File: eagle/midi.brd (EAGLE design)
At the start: 62.5 x 83.8 mm, 31 parts, among them CON1 EXPANSION-PORT, IC1 74LS14, IC2 6N138, IC4 74LS02, IC5 74LS74, IC6 74AHCT1G32DBV, IC7 74LS273, IC8 SST39SF040, IC9 74LS00D, Q1 2MHz

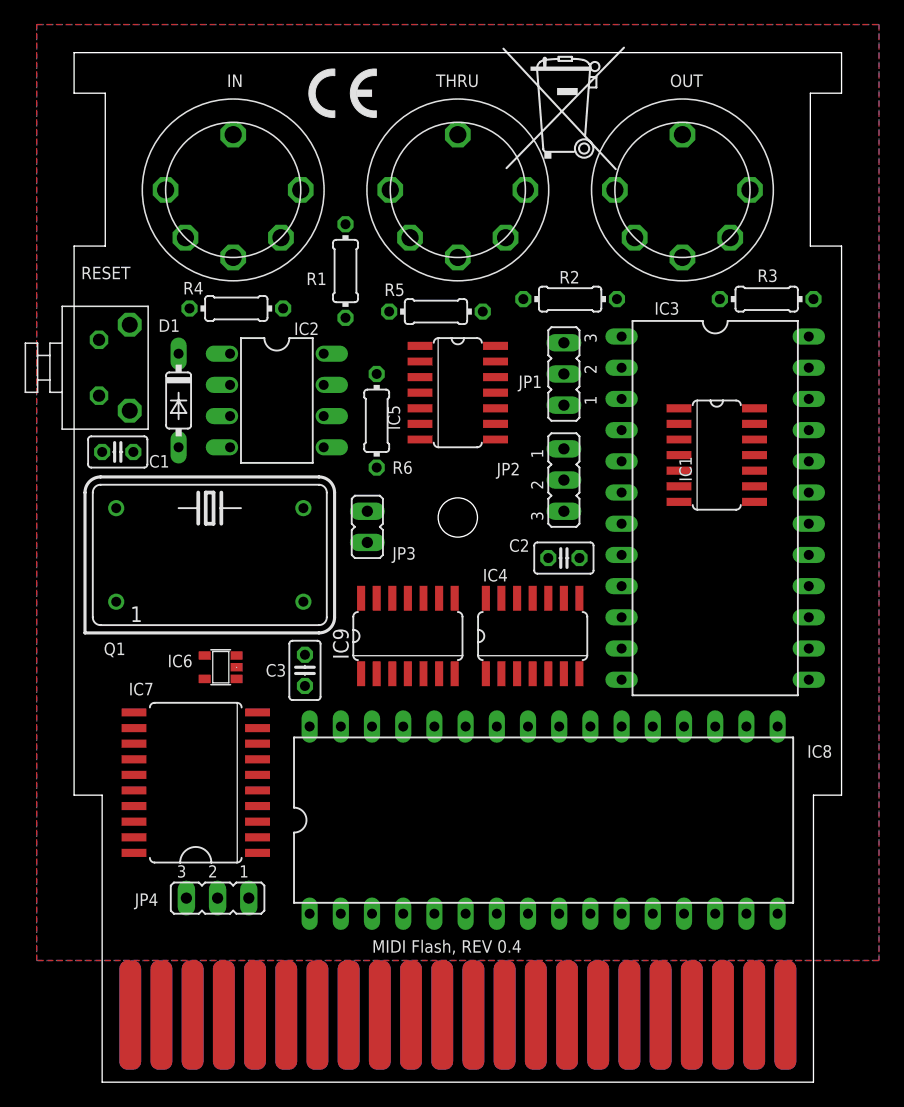
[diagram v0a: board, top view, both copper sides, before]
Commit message: version 0.5 with additonal 74LS00
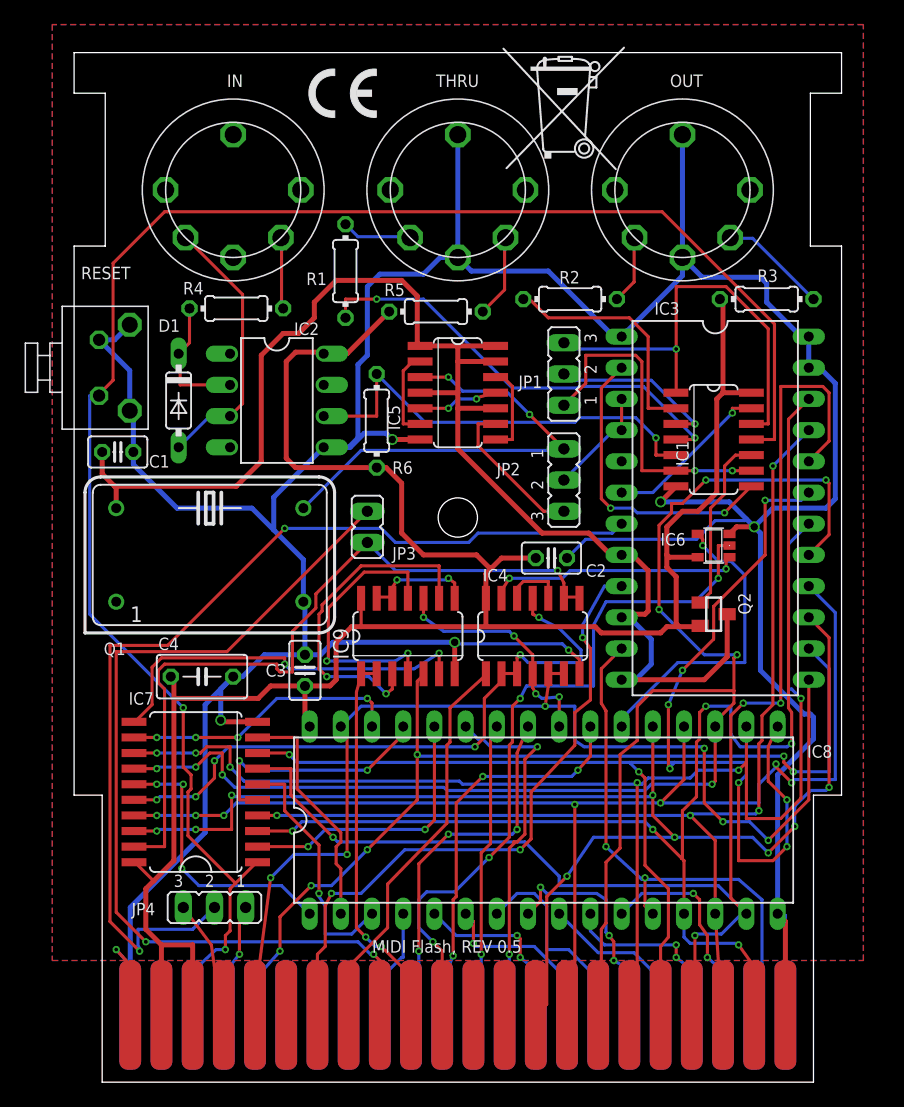
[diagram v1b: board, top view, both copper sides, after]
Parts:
- added C4: 10u, rcl:C050-035X075
- added Q2: DMP2100U, transistor-power:SUPER-SOT3
- moved IC6 41.3 mm to (50.0, 43.9)
- moved IC1 1.30 mm to (50.0, 52.6)
- moved C2 1.02 mm to (36.8, 42.9), turned to 0 degrees
- moved JP4 0.80 mm to (9.40, 14.5)
- moved IC7 0.76 mm to (7.87, 23.9)
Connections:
- removed net OE: IC4.4, IC8.24
- removed net ROMH: CON1.B
- new net !RW: IC4.4, IC8.24, IC9.10
- new net 5V-SW: C1.1, IC3.10, IC3.12, IC3.8, IC5.1, IC5.10, IC5.13, IC5.14, IC5.4, Q1.14, Q2.3
- new net N$30: IC9.11, IC9.4
- new net N$35: IC1.10, Q2.1
- new net N$9: IC9.12, IC9.13, IC9.8
- net +5V: now also C4.1, Q2.2; no longer C1.1, IC3.10, IC3.12, IC3.8, IC5.1, IC5.10, IC5.13, IC5.14, IC5.4, Q1.14
- net GND: now also C4.2; no longer IC1.11, IC9.10, IC9.12, IC9.13, IC9.9
- net N$8: now also IC9.9; no longer IC9.4
- net RESET: now also IC1.11
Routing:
- net GND: track 0.00 -> 318.6 mm, vias 0 -> 7
- net +5V: track 0.00 -> 177.3 mm
- net RESET: track 0.00 -> 142.7 mm, vias 0 -> 2
- net D5: track 0.00 -> 133.6 mm, vias 0 -> 8
- net 5V-SW: track 0.00 -> 117.1 mm
- net D2: track 0.00 -> 115.3 mm, vias 0 -> 4
- net D3: track 0.00 -> 115.0 mm, vias 0 -> 9
- net D7: track 0.00 -> 108.5 mm, vias 0 -> 9
- net D4: track 0.00 -> 108.5 mm, vias 0 -> 6
- net D0: track 0.00 -> 105.3 mm, vias 0 -> 5
- net D6: track 0.00 -> 102.0 mm, vias 0 -> 7
- net RW: track 0.00 -> 91.5 mm, vias 0 -> 6
- net D1: track 0.00 -> 90.8 mm, vias 0 -> 4
- net IRQ: track 0.00 -> 81.4 mm, vias 0 -> 2
- net S02: track 0.00 -> 79.5 mm, vias 0 -> 6
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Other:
- board text added: "MIDI Flash, REV 0.5"
- board text removed: "MIDI Flash, REV 0.4"

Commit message: revision 1.0
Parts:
- added C10, C5, C6, C7, C8, C9: 100n, rcl:C0805
- added C11, C12: 1n, rcl:C0805
- added D2, D3: BAV99, diode:SOT23
- added R7: 10k, rcl:R0805
- C1, C2, C3: device rcl:C025-025X050 -> rcl:C0805
- C4: device rcl:C050-035X075 -> rcl:C0805
- D1: value 1N914 -> BAV99; device diode:DO35-7 -> diode:SOT23
- R1, R2, R3, R4, R5, R6: device rcl:0204/7 -> rcl:R1206
- moved C1 46.4 mm to (43.7, 32.3)
- moved C2 21.9 mm to (52.1, 58.7), turned to 180 degrees
- moved C3 19.8 mm to (4.06, 18.5), turned to 0 degrees
- moved C4 19.4 mm to (2.79, 14.7), turned to 270 degrees
- moved U$1 17.3 mm to (49.5, 74.2)
- moved U$2 16.0 mm to (1.02, 79.5)
- moved R6 3.34 mm to (22.1, 57.4), turned to 90 degrees
- moved IC7 2.79 mm to (7.87, 26.7)
- moved R5 2.54 mm to (24.9, 63.1)
- moved R3 2.18 mm to (55.6, 65.8)
- moved IC3 2.04 mm to (50.0, 49.0)
- moved R2 1.78 mm to (38.4, 65.8), turned to 270 degrees
- moved IC6 1.78 mm to (50.0, 45.7)
- moved D1 1.40 mm to (6.35, 57.1), turned to 0 degrees
- moved Q2 1.37 mm to (48.8, 38.9), turned to 180 degrees
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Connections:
- removed net N$2: D1.C, IC2.2, R4.1
- new net N$37: D1.2, D1.3, IC2.2, R4.1
- net +5V: now also C10.1, C7.1, C8.1, C9.1, D2.2, D3.2, R7.1
- net 5V-SW: now also C5.1, C6.1
- net GND: now also C10.2, C11.2, C12.2, C5.2, C6.2, C7.2, C8.2, C9.2, D2.1, D3.1
- net N$16: now also C12.1, D3.3
- net N$28: now also C11.1, D2.3
- net N$3: now also D1.1; no longer D1.A
- net N$35: now also R7.2
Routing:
- net GND: track 318.6 -> 509.2 mm, vias 7 -> 23
- net N$22: track 22.9 -> 78.1 mm, vias 3 -> 6
- net +5V: track 177.3 -> 232.1 mm
- net D1: track 90.8 -> 133.5 mm, vias 4 -> 8
- net EXROM: track 73.9 -> 45.7 mm, vias 2 -> 4
- net N$5: track 27.4 -> 53.5 mm, vias 2 -> 3
- net D7: track 108.5 -> 83.2 mm, vias 9 -> 8
- net D5: track 133.6 -> 108.7 mm, vias 8 -> 7
- net N$37: track 0.00 -> 24.2 mm
- net N$28: track 5.72 -> 28.2 mm, vias 0 -> 2
- net N$23: track 31.5 -> 52.4 mm, vias 2 -> 4
- net N$16: track 5.60 -> 24.7 mm, vias 0 -> 1
- net N$12: track 36.4 -> 53.7 mm
- net RESET: track 142.7 -> 127.3 mm, vias 2 -> 10
- net D3: track 115.0 -> 99.8 mm, vias 9 -> 3
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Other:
- board text added: "FRANK-BUSS.DE"
- board text added: "KERBEROS, REV 1.0"
- board text removed: "MIDI Flash, REV 0.5"

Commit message: circuit rev B with CPLD
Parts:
- removed C10, C2, C5, C6, C7, C8, C9: 100n, rcl:C0805
- removed C11, C12: 1n, rcl:C0805
- removed C4: 10u, rcl:C0805
- removed D1, D2, D3: BAV99, diode:SOT23
- removed IC6: 74AHCT1G32DBV, 74xx-little-de:SOT23-5
- removed IC7: 74LS273, 74xx-eu:SO20W
- removed IC8: SST39SF040, flash:DIL32
- removed IC9: 74LS00D, 74xx-eu:SO14
- removed JP2, JP4: (no value), jumper:JP2
- removed JP3: (no value), jumper:JP1
- removed Q1: 2MHz, crystal:DIL14S
- removed Q2: DMP2100U, transistor-power:SUPER-SOT3
- added 3V3, AUX, GND, TCK, TDI, TDO, TMS: LSP10, solpad:LSP10
- added C13, C14, C17, C18, C19, C20, C21, C26, C28, C37: 100n, rcl:C0402
- added C15, C16: 1n, rcl:C0402
- added C22: 10u, rcl:C0805
- added C24: 1u, rcl:C0805
- added D4, D5, D6: BAV99, diode:SOT23
- added IC11: (no value), micro-motorola:DIL24
- added IC12: 74LS14, 74xx-eu:SO14
- added IC16: 74LVC8T245, 74lvc8t245:TSSOP24
- added IC18: MCP1703CB, linear:SOT23
- added LED1, LED2: (no value), led:LED3MM
- added R10, R11, R12, R13, R8, R9: 220, rcl:R1206
- added R14, R17, R18: 10k, rcl:R0402
- added R15, R16: 4k7, rcl:R0402
- C1, C3: device rcl:C0805 -> rcl:C0402
- IC1: value 74LS14 -> SST39VF1681; device 74xx-eu:SO14 -> flash:TSOP48
- IC2: value 6N138 -> XC9572XL_TQ100; device optocoupler:DIL08 -> xc9572xl-tq100:TQ100
- IC3: value (none) -> 6N138SMD; device micro-motorola:DIL24 -> 6n138:SO8-GW300
- IC4: value 74LS02 -> 12MHz; device 74xx-eu:SO14 -> cartridge:ASE
- IC5: value 74LS74 -> CY61228EV30; device 74xx-eu:SO14 -> CY62128EV30:TSOP8X16
- JP1: device jumper:JP2 -> jumper:JP1
- R1, R2, R3: value 220 -> 10k; device rcl:R1206 -> rcl:R0402
- R4, R5: value 220 -> 1k; device rcl:R1206 -> rcl:R0402
- R6: value 330 -> 10k; device rcl:R1206 -> rcl:R0402
- R7: value 10k -> 220; device rcl:R0805 -> rcl:R1206
- moved JP1 49.0 mm to (18.4, 12.9), turned to 270 degrees
- moved R1 47.4 mm to (3.05, 23.4)
- moved IC3 39.6 mm to (10.7, 52.8), turned to 0 degrees
- moved IC5 34.6 mm to (51.1, 29.2), turned to 180 degrees
- moved IC2 34.2 mm to (34.0, 27.7), turned to 90 degrees
- moved R7 33.9 mm to (20.3, 50.8), turned to 270 degrees
- moved C3 22.9 mm to (23.7, 30.2), turned to 270 degrees
- moved R2 14.9 mm to (52.3, 60.7), turned to 0 degrees
- moved R5 13.3 mm to (38.1, 61.5)
- moved IC4 13.2 mm to (37.8, 49.5), turned to 270 degrees
- moved C1 12.8 mm to (56.4, 30.5), turned to 270 degrees
- moved R4 9.43 mm to (19.8, 61.5), turned to 180 degrees
- moved R6 6.31 mm to (17.3, 53.3)
- moved R3 5.08 mm to (55.6, 60.7), turned to 0 degrees
- moved IC1 4.10 mm to (51.6, 49.0), turned to 90 degrees
- renumbered CON1 to CON2, RESET to RESET1
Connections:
- removed net !RW: IC4.4, IC8.24, IC9.10
- removed net 5V-SW: C1.1, C5.1, C6.1, IC3.10, IC3.12, IC3.8, IC5.1, IC5.10, IC5.13, IC5.14, IC5.4, Q1.14, Q2.3
- removed net CE: IC6.4, IC8.22
- removed net N$10: IC1.2, R2.2
- removed net N$11: IC1.3, JP1.2
- removed net N$12: IC1.4, R1.2
- removed net N$14: IC3.3, IC3.4, JP2.2
- removed net N$15: IC1.8, IC3.2
- removed net N$16: C12.1, D3.3, OUT.5, R2.1
- removed net N$17: IC7.2, IC8.28
- removed net N$19: IC7.6, IC8.3
- removed net N$20: IC7.9, IC8.2
- removed net N$21: IC7.12, IC8.30
- removed net N$22: IC7.15, IC8.1
- removed net N$23: IC7.11, IC9.6
- removed net N$24: IC4.10, IC4.12
- removed net N$25: IC1.13, IC3.6
- removed net N$26: CON2.4, JP4.3
- removed net N$27: CON2.D, JP4.1
- removed net N$28: C11.1, D2.3, R1.1, THRU.5
- removed net N$29: IC4.13, IC6.1
- removed net N$30: IC9.11, IC9.4
- removed net N$31: IC5.2, IC5.6
- removed net N$32: IC5.12, IC5.8
- removed net N$33: IC5.3, JP2.1, Q1.8
- removed net N$34: IC5.11, IC5.5
- removed net N$35: IC1.10, Q2.1, R7.2
- removed net N$36: IC5.9, JP2.3
- removed net N$37: D1.2, D1.3, IC2.2, R4.1
- removed net N$9: IC9.12, IC9.13, IC9.8
- removed net Q7: IC4.11, IC4.2, IC4.3, IC7.16
- removed net Q8: IC4.8, IC4.9, IC7.19, JP3.1
- new net +3V3: 3V3.MP, C1.1, C17.1, C18.1, C19.1, C24.1, C26.1, C28.1, C3.1, C37.1, IC1.12, IC1.37, IC16.1, IC18.2, IC2.26, IC2.38, IC2.5, IC2.51, IC2.57, IC2.88, IC2.98, IC4.4, IC5.6, IC5.8, R14.2, R15.1, R16.1, R18.2, R2.1
- new net 6850-CS2: IC11.9, IC2.63, R1.1
- new net 6850-IRQ: IC11.7, IC2.58
- new net 6850-RS: IC11.11, IC2.64
- new net 6850-RW: IC11.13, IC2.65
- new net 6850-RX/TX-CLK: IC11.3, IC11.4, IC2.55
- new net 6850-RXDATA: IC11.2, IC12.6, IC2.54
- new net 6850-TXDATA: IC11.6, IC12.3, IC2.56
- new net A13: CON2.J, IC2.77
- new net A14: CON2.H, IC2.74
- new net A15: CON2.F, IC2.71
- new net AT0: IC1.45, IC2.14, IC5.20
- new net AT1: IC1.25, IC2.13, IC5.19
- new net AT10: IC1.7, IC2.16, IC5.31
- new net AT11: IC1.6, IC2.22, IC5.11
- new net AT12: IC1.5, IC2.23, IC5.12
- new net AT13: IC1.4, IC2.25, IC5.13
- new net AT14: IC1.3, IC2.28, IC5.14
- new net AT15: IC1.2, IC2.29, IC5.15
- new net AT16: IC1.1, IC2.30, IC5.16
- new net AT17: IC1.48, IC2.59
- new net AT18: IC1.17, IC2.37
- new net AT19: IC1.16, IC2.36
- new net AT2: IC1.24, IC2.12, IC5.18
- new net AT20: IC1.9, IC2.33
- new net AT3: IC1.23, IC2.11, IC5.17
- new net AT4: IC1.22, IC2.20, IC5.10
- new net AT5: IC1.21, IC2.42, IC5.1
- new net AT6: IC1.20, IC2.41, IC5.2
- new net AT7: IC1.19, IC2.40, IC5.3
- new net AT8: IC1.18, IC2.39, IC5.4
- new net AT9: IC1.8, IC2.32, IC5.7
- new net BA: CON2.12
- new net DIR: IC16.2, IC2.1, R17.1
- new net DMA: CON2.13
- new net DOT-CLOCK: CON2.6
- new net DT0: IC1.29, IC16.3, IC2.3, IC5.29
- new net DT1: IC1.31, IC16.4, IC2.4, IC5.28
- new net DT2: IC1.33, IC16.5, IC2.6, IC5.27
- new net DT3: IC1.35, IC16.6, IC2.8, IC5.26
- new net DT4: IC1.38, IC16.7, IC2.9, IC5.25
- new net DT5: IC1.40, IC16.8, IC2.10, IC5.23
- new net DT6: IC1.42, IC16.9, IC2.18, IC5.22
- new net DT7: IC1.44, IC16.10, IC2.17, IC5.21
- new net FLASH-CE: IC1.26, IC2.60, R14.1
- new net LED1: IC2.53, R4.1
- new net LED2: IC2.52, R5.1
- new net MIDI-OUT-INVERTED: IC12.4, IC12.9
- new net MIDI-THRU: IC12.13, IC2.49
- new net N$2: IC2.27, IC4.3
- new net N$38: IN.4, R8.2
- new net N$39: IC12.1, IC3.6, R7.2
- new net N$40: OUT.4, R11.1
- new net N$41: R10.1, THRU.4
- new net N$42: C16.1, D6.3, OUT.5, R13.1
- new net N$43: C15.1, D5.3, R12.1, THRU.5
- new net N$44: IC12.8, R13.2
- new net N$45: IC12.10, R12.2
- new net N$47: D4.1, IC3.3, IN.5
- new net N$48: D4.2, D4.3, IC3.2, R8.1
- new net NMI: CON2.D, IC2.68
- new net OE: IC1.28, IC2.61, IC5.32
- new net RAM-CE: IC2.15, IC5.30, R18.1
- new net ROMH: CON2.B, IC2.66
- new net TCK: IC2.48, TCK.MP
- new net TDI: IC2.45, R15.2, TDI.MP
- new net TDO: IC2.83, TDO.MP
- new net TMS: IC2.47, R16.2, TMS.MP
- new net WE: IC1.11, IC2.35, IC5.5
- net +5V: now also C13.1, C14.1, C20.1, C21.1, C22.1, D5.2, D6.2, IC11.10, IC11.12, IC11.8, IC12.14, IC16.23, IC16.24, IC18.3, IC3.8, R1.2, R10.2, R11.2, R9.1; no longer C10.1, C2.1, C3.1, C4.1, C7.1, C8.1, C9.1, D2.2, D3.2, IC1.14, IC2.8, IC4.14, IC6.5, IC7.20, IC8.32, IC9.14, Q2.2, R3.2, R5.2, R6.2, R7.1
- net A0: now also IC2.99; no longer IC3.11, IC8.12
- net A1: now also IC2.97; no longer IC8.11
- net A10: now also IC2.86; no longer IC8.23
- net A11: now also IC2.82; no longer IC8.25
- net A12: now also IC2.79; no longer IC8.4
- net A2: now also IC2.96; no longer IC8.10
- net A3: now also IC2.95; no longer IC8.9
- net A4: now also IC2.94; no longer IC8.8
- net A5: now also IC2.93; no longer IC8.7
- net A6: now also IC2.92; no longer IC8.6
- net A7: now also IC2.91; no longer IC8.5
- net A8: now also IC2.90; no longer IC8.27
- net A9: now also IC2.89; no longer IC8.26
- net D0: now also IC11.22, IC16.21; no longer IC3.22, IC7.3, IC8.13
- net D1: now also IC11.21, IC16.20; no longer IC3.21, IC7.4, IC8.14
- net D2: now also IC11.20, IC16.19; no longer IC3.20, IC7.7, IC8.15
- net D3: now also IC11.19, IC16.18; no longer IC3.19, IC7.8, IC8.17
- net D4: now also IC11.18, IC16.17; no longer IC3.18, IC7.13, IC8.18
- net D5: now also IC11.17, IC16.16; no longer IC3.17, IC7.14, IC8.19
- net D6: now also IC11.16, IC16.15; no longer IC3.16, IC7.17, IC8.20
- net D7: now also IC11.15, IC16.14; no longer IC3.15, IC7.18, IC8.21
- net EXROM: now also JP1.1; no longer JP3.2
- net GAME: now also IC2.78; no longer IC4.1
- net GND: now also C13.2, C14.2, C15.2, C16.2, C17.2, C18.2, C19.2, C20.2, C21.2, C22.2, C24.2, C26.2, C28.2, C37.2, D5.1, D6.1, GND.MP, IC1.27, IC1.46, IC11.1, IC11.23, IC11.24, IC12.7, IC16.11, IC16.12, IC16.13, IC16.22, IC18.1, IC2.100, IC2.21, IC2.31, IC2.44, IC2.62, IC2.69, IC2.75, IC2.84, IC3.5, IC4.2, IC5.24, LED1.K, LED2.K, R17.2, R3.2, R6.1; no longer C10.2, C11.2, C12.2, C2.2, C4.2, C5.2, C6.2, C7.2, C8.2, C9.2, D2.1, D3.1, IC1.7, IC2.5, IC3.1, IC3.23, IC3.24, IC4.7, IC5.7, IC6.3, IC7.10, IC8.16, IC9.7, Q1.7
- net IO1: now also IC2.76; no longer IC3.9
- net IO2: now also IC2.85; no longer IC9.1, IC9.2
- net IRQ: now also CON2.4, IC2.70; no longer IC3.7, JP4.2
- net N$1: now also IC3.7, R6.2; no longer IN.4, R4.2
- net N$13: now also IC1.14, R2.2, R3.1; no longer IC1.1, IC1.12, JP1.3
- net N$18: now also LED2.A, R5.2; no longer IC7.5, IC8.29
- net N$3: now also R7.1, R9.2; no longer D1.1, IC2.3, IN.5
- net N$4: now also IC12.11, IC12.12; no longer IC1.5, IC2.6, R6.1
- net N$5: now also IC12.2, IC12.5; no longer IC1.6, IC1.9, JP1.1
- net N$6: now also LED1.A, R4.2; no longer OUT.4, R3.1
- net N$7: now also IC2.81, JP1.2; no longer R5.1, THRU.4
- net N$8: now also AUX.MP, IC2.50; no longer IC9.3, IC9.9
- net RESET: now also IC2.67; no longer IC1.11, IC7.1
- net ROML: now also IC2.87; no longer IC6.2
- net RW: now also IC2.72; no longer IC3.13, IC4.5, IC4.6, IC8.31
- net S02: now also IC11.14; no longer IC3.14, IC9.5
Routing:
- net GND: track 509.2 -> 800.6 mm, vias 23 -> 34
- net +3V3: track 0.00 -> 230.4 mm, vias 0 -> 3
- net 5V-SW: track 117.5 -> 0.00 mm, vias 2 -> 0
- net N$22: track 78.1 -> 0.00 mm, vias 6 -> 0
- net D1: track 133.5 -> 57.5 mm, vias 8 -> 1
- net OE: track 0.00 -> 72.5 mm, vias 0 -> 5
- net S02: track 85.9 -> 18.0 mm, vias 4 -> 2
- net 6850-TXDATA: track 0.00 -> 64.4 mm, vias 0 -> 3
- net RW: track 91.7 -> 29.2 mm, vias 5 -> 0
- net D5: track 108.7 -> 46.4 mm, vias 7 -> 1
- net LED1: track 0.00 -> 61.8 mm, vias 0 -> 4
- net DT0: track 0.00 -> 60.1 mm, vias 0 -> 2
- net AT2: track 0.00 -> 59.7 mm, vias 0 -> 2
- net FLASH-CE: track 0.00 -> 58.8 mm, vias 0 -> 5
- net DT1: track 0.00 -> 58.3 mm, vias 0 -> 2
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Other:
- outline, holes or cut-outs redrawn
- board text added: "KERBEROS, REV B"
- board text removed: "KERBEROS, REV 1.0"

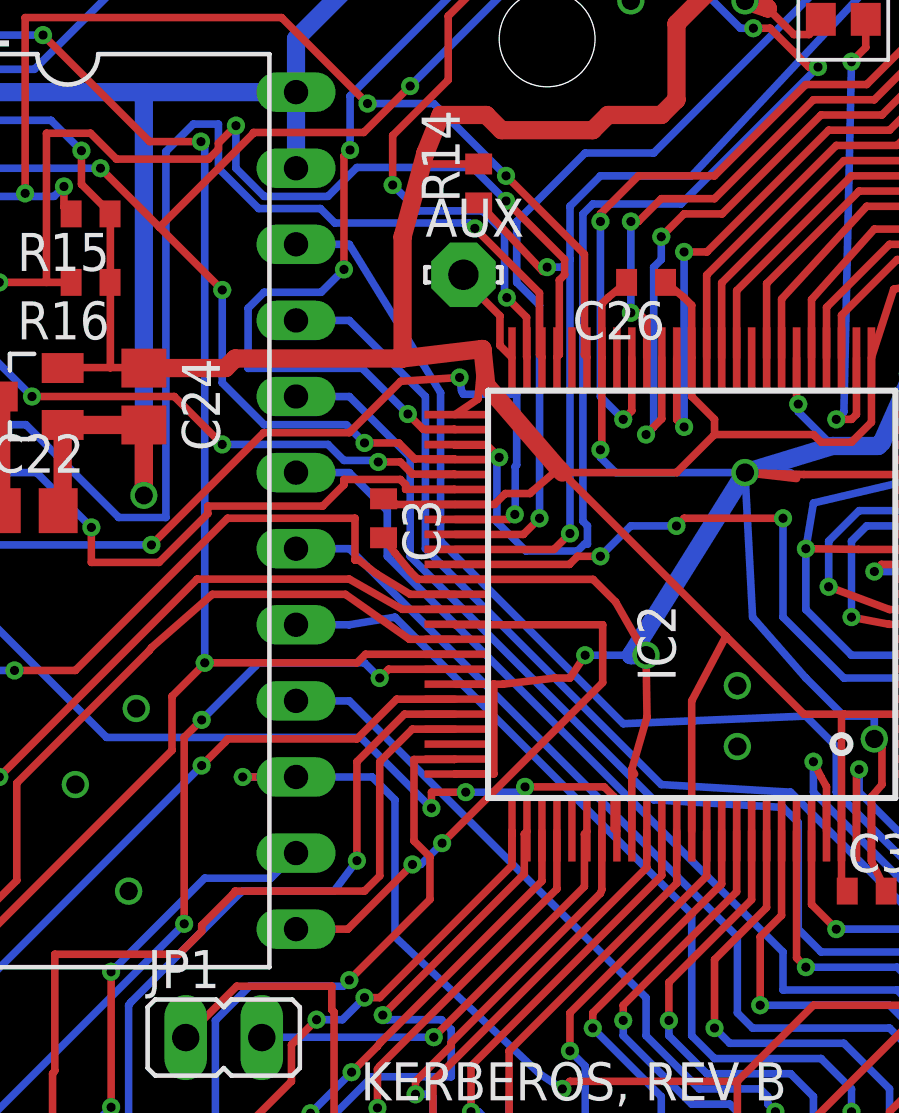
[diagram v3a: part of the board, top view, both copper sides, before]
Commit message: first working prototype with CPLD
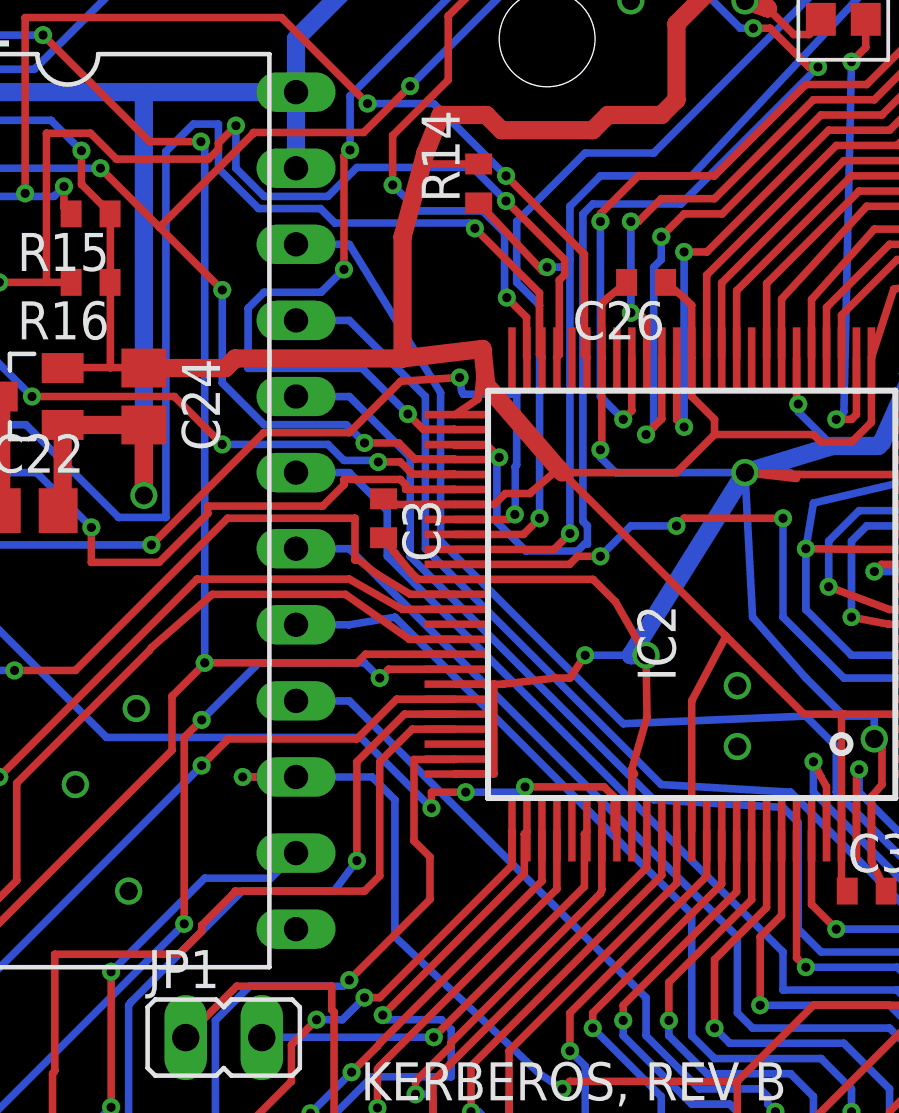
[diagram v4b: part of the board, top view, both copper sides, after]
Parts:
- removed AUX: LSP10, solpad:LSP10
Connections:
- removed net 6850-RW: IC11.13, IC2.65
- removed net N$8: AUX.MP, IC2.50
- net BA: now also IC2.65
- net RW: now also IC11.13
- net S02: now also IC2.50
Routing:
- net 6850-RW: track 20.5 -> 0.00 mm, vias 2 -> 0
- net N$8: track 3.44 -> 0.00 mm
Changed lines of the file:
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@@
 <element name="R14" library="rcl" package="R0402" value="10k" x="26.924" y="41.402" rot="R90"/>
 <element name="R18" library="rcl" package="R0402" value="10k" x="57.404" y="32.766"/>
-<element name="AUX" library="solpad" package="LSP10" value="LSP10" x="26.416" y="38.354"/>
 <element name="JP1" library="jumper" package="JP1" value="" x="18.415" y="12.8905" rot="R270"/>
 </elements>
@@
 <via x="14.6558" y="15.0876" extent="1-16" drill="0.3048"/>
 <via x="14.6558" y="10.5664" extent="1-16" drill="0.3048"/>
+<contactref element="IC2" pad="50"/>
+<wire x1="20.828" y1="19.05" x2="28.036" y2="35.586" width="0" layer="19" extent="1-1"/>
 </signal>
 <signal name="RW">
@@
 <wire x1="18.7198" y1="17.6784" x2="18.796" y2="17.78" width="0.254" layer="1"/>
 <wire x1="12.7762" y1="11.7856" x2="12.7" y2="11.684" width="0.254" layer="1"/>
+<contactref element="IC11" pad="13"/>
+<wire x1="18.796" y1="17.78" x2="20.828" y2="16.51" width="0" layer="19" extent="1-1"/>
 </signal>
 <signal name="A0">
@@
 <signal name="BA">
 <contactref element="CON2" pad="12"/>
+<contactref element="IC2" pad="65"/>
+<wire x1="30.48" y1="5.715" x2="26.136" y2="26.686" width="0" layer="19" extent="1-1"/>
 </signal>
 <signal name="DOT-CLOCK">
@@
 <wire x1="10.922" y1="21.59" x2="8.382" y2="19.05" width="0.254" layer="16"/>
 <wire x1="5.588" y1="19.05" x2="8.382" y2="19.05" width="0.254" layer="16"/>
-</signal>
-<signal name="6850-RW">
-<contactref element="IC11" pad="13"/>
-<contactref element="IC2" pad="65"/>
-<wire x1="31.0642" y1="26.67" x2="26.1366" y2="26.67" width="0.254" layer="1"/>
-<wire x1="31.0642" y1="24.7396" x2="31.0642" y2="26.67" width="0.254" layer="1"/>
-<wire x1="25.7048" y1="19.3802" x2="31.0642" y2="24.7396" width="0.254" layer="1"/>
-<wire x1="24.9936" y1="18.669" x2="25.7048" y2="19.3802" width="0.254" layer="16"/>
-<wire x1="24.7142" y1="18.669" x2="24.9936" y2="18.669" width="0.254" layer="16"/>
-<wire x1="22.5552" y1="16.51" x2="24.7142" y2="18.669" width="0.254" layer="1"/>
-<wire x1="20.828" y1="16.51" x2="22.5552" y2="16.51" width="0.254" layer="1"/>
-<wire x1="26.1366" y1="26.67" x2="26.136" y2="26.686" width="0.254" layer="1"/>
-<via x="25.7048" y="19.3802" extent="1-16" drill="0.3048"/>
-<via x="24.7142" y="18.669" extent="1-16" drill="0.3048"/>
 </signal>
 <signal name="+3V3">
@@
 <via x="27.6098" y="32.258" extent="1-16" drill="0.3048"/>
 </signal>
-<signal name="N$8">
-<contactref element="IC2" pad="50"/>
-<contactref element="AUX" pad="MP"/>
-<wire x1="27.6352" y1="35.9918" x2="28.0162" y2="35.6108" width="0.254" layer="1"/>
-<wire x1="27.6352" y1="36.9824" x2="27.6352" y2="35.9918" width="0.254" layer="1"/>
-<wire x1="26.416" y1="38.2016" x2="27.6352" y2="36.9824" width="0.254" layer="1"/>
-<wire x1="26.416" y1="38.354" x2="26.416" y2="38.2016" width="0.254" layer="1"/>
-<wire x1="28.0162" y1="35.6108" x2="28.036" y2="35.586" width="0.254" layer="1"/>
-</signal>
 <signal name="N$7">
